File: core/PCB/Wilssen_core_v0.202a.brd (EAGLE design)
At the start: 25.4 x 64.8 mm, 38 parts, among them Q1 8Mhz, T1 BC849, U1 MAX1555, U2 3.3V, U3 ATMEGA168/ATMEGA328, X1 USBSMD

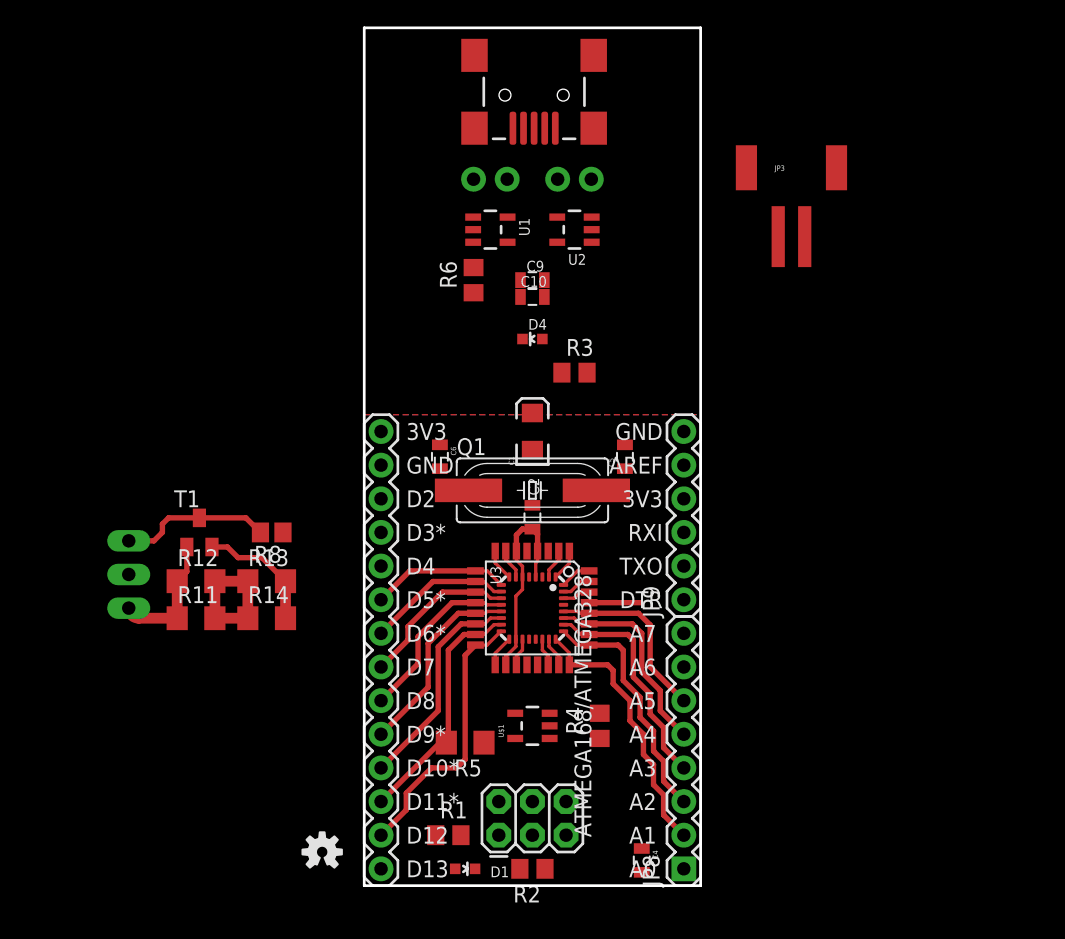
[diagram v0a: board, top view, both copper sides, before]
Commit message: CCS2 added
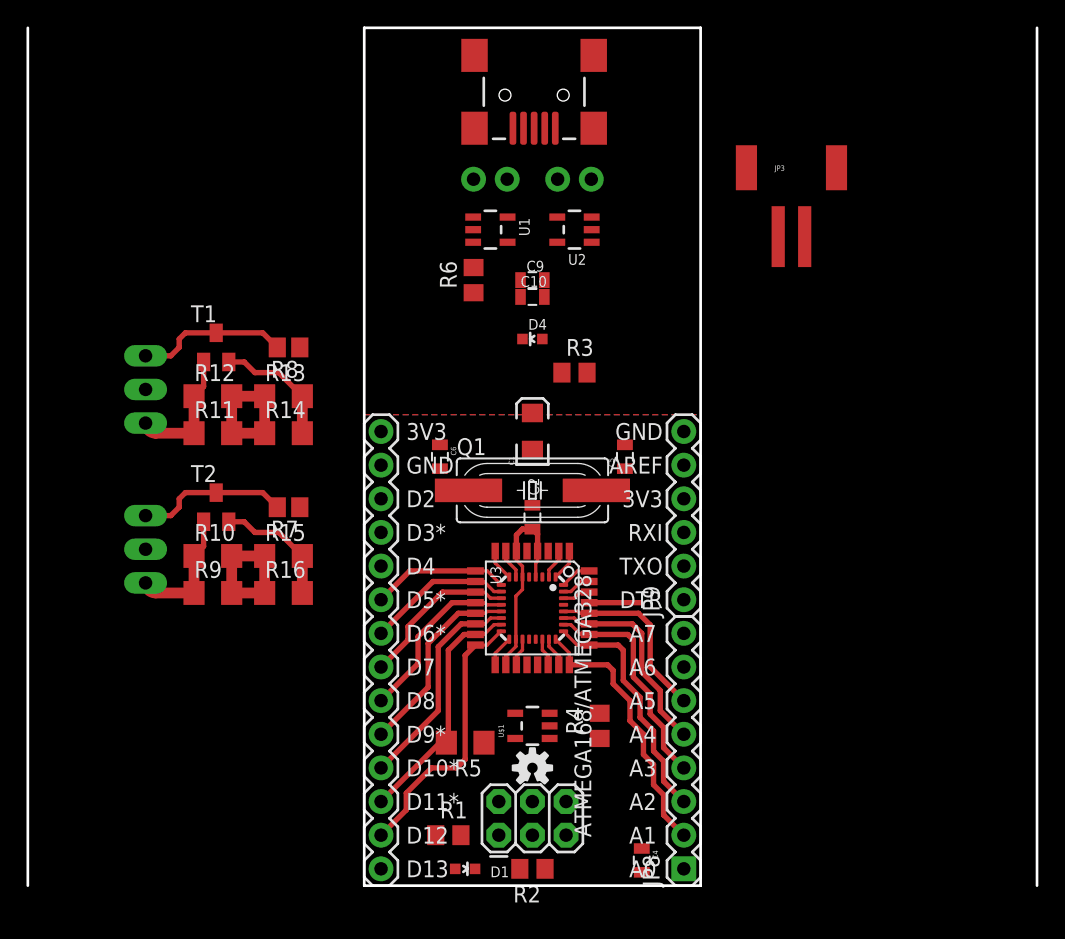
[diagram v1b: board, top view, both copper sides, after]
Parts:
- added FET2: IRLZ, transistor-power:TO220BV
- added R10, R15, R16, R9: 3R3, resistor:R1206
- added R7: 10k, resistor:R0805
- added T2: BC849, transistor:SOT23
- moved LOGO1 17.1 mm to (43.2, 8.89)
- moved FET1 14.0 mm to (11.4, 37.5)
- moved R12 14.0 mm to (19.1, 37.0)
- moved R13 14.0 mm to (24.4, 37.0)
- moved R8 14.0 mm to (24.8, 40.6)
- moved T1 14.0 mm to (19.3, 40.6)
- moved R11 14.0 mm to (19.1, 34.2)
- moved R14 14.0 mm to (24.4, 34.2)
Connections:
- new net GATE2: FET2.G, R7.2, T2.3
- new net LED-OUT_G: FET2.D
- new net NS$2: R10.2, R15.1, R16.1, R9.2
- new net SRC2: FET2.S, R10.1, R9.1, T2.1
- net D5_LED-G: now also R7.1
- net GND: now also R15.2, R16.2, T2.2
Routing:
- net GATE2: track 0.00 -> 11.5 mm
- net NS$2: track 0.00 -> 10.5 mm
- net SRC2: track 0.00 -> 9.65 mm
- net GND: track 9.42 -> 18.8 mm
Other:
- board size 25.4 x 64.8 mm -> 76.2 x 64.8 mm
